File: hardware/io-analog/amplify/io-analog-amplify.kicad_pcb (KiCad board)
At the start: 2 copper layers, 60 x 60 mm, 22 parts, among them J1 IO EXTENSION, J2 DIMMER_B, J5 12V_A, J6 12V_B, U1 LM317T, U2 74LS164, U3 TLC7226A, U4 LM324A

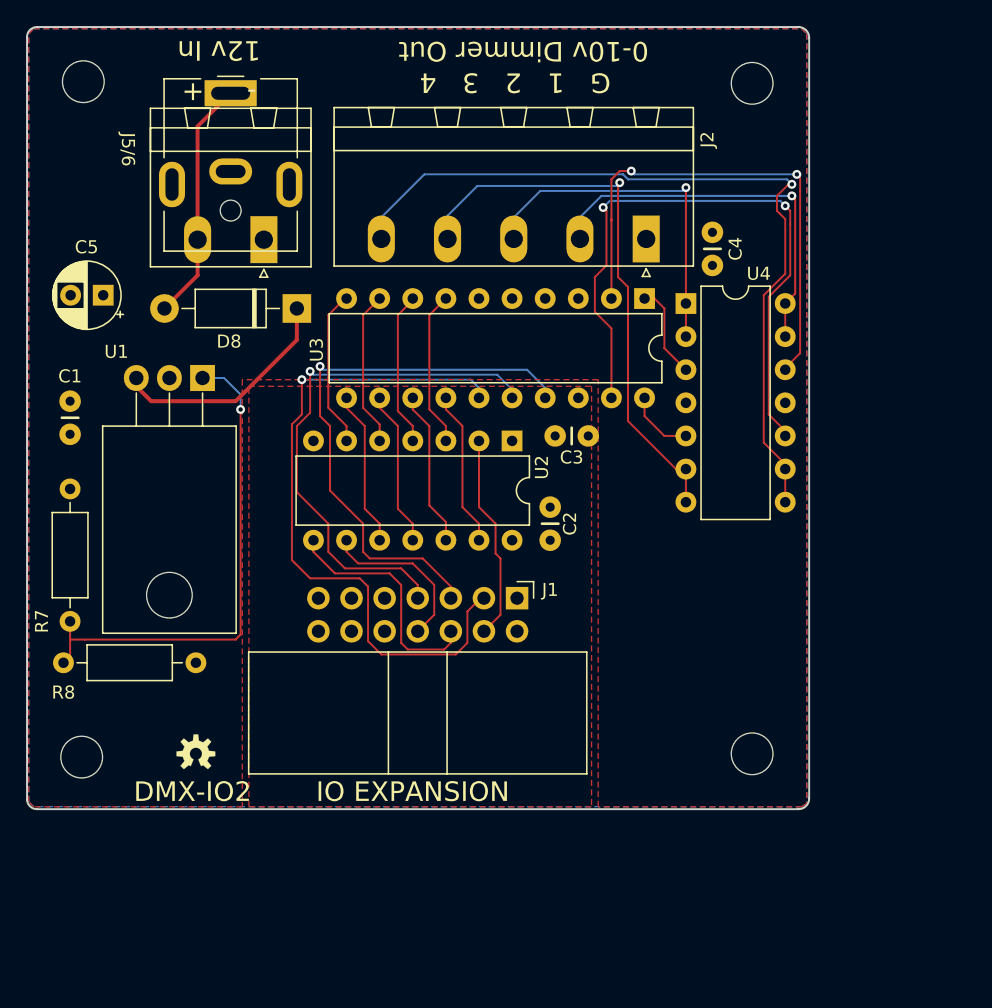
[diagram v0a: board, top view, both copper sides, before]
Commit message: Make io-analog a stackable family io-analog-core handles D to A io-analog-amplify handles voltage output io-analog-pwm handles pwm output for leds, drive display pro io-analog-led handles 5v pwm output for iot, drive display pro
Refactor display-pro to work with io-analog-pwm
Add correct coax power connector
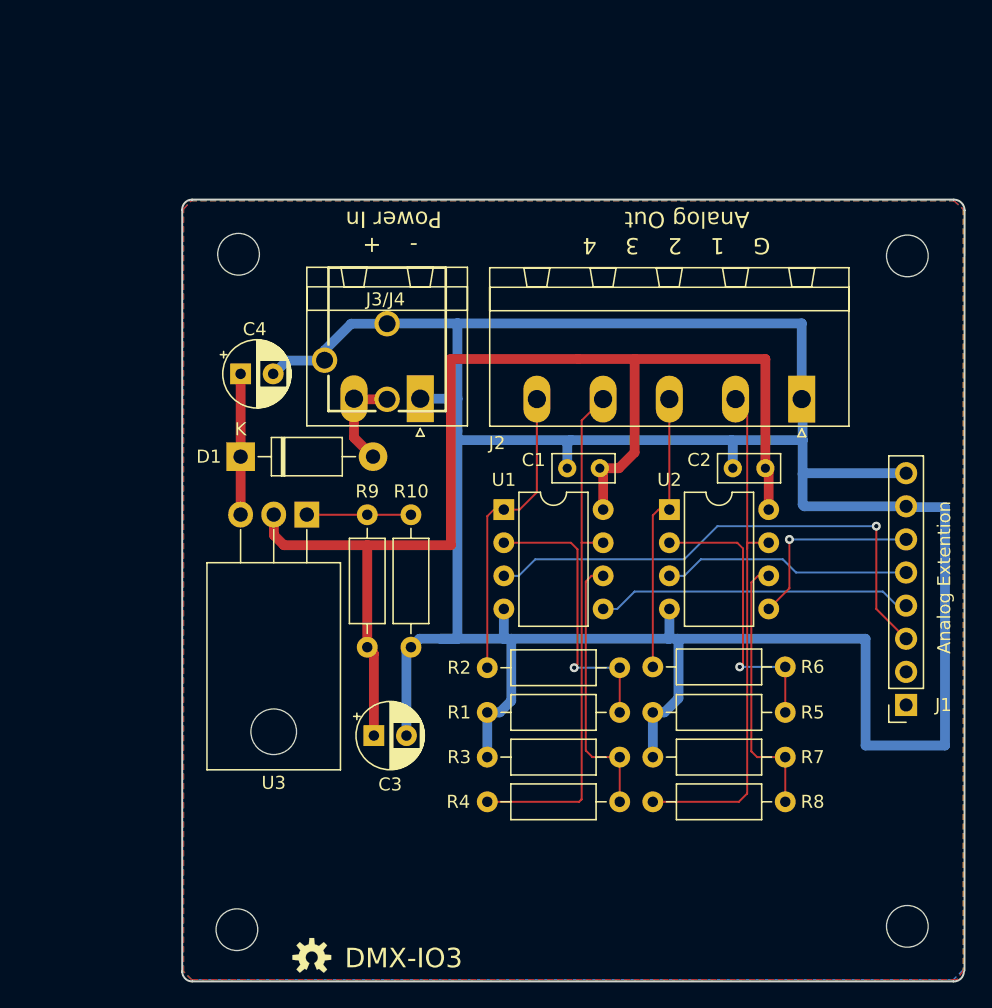
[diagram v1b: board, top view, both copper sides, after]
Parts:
- removed C5: 10uF, Capacitor_THT:CP_Radial_D5.0mm_P2.50mm
- removed D8: 1N5819, Diode_THT:D_DO-41_SOD81_P10.16mm_Horizontal
- removed J5: 12V_A, Connector_BarrelJack:BarrelJack_CUI_PJ-063AH_Horizontal
- removed J6: 12V_B, Connector_Phoenix_MSTB:PhoenixContact_MSTBA_2,5_2-G-5,08_1x02_P5.08mm_Horizontal
- removed U4: LM324A, Package_DIP:DIP-14_W7.62mm
- added D1: 1N5819, Diode_THT:D_DO-41_SOD81_P10.16mm_Horizontal, F.Cu at (130.8, 93.5)
- added J3: Power, Connector_Phoenix_MSTB:PhoenixContact_MSTBA_2,5_2-G-5,08_1x02_P5.08mm_Horizontal, F.Cu at (144.6, 89.1)
- added J4: Power, Connectors:POWER_JACK_PTH_BREAD, F.Cu at (142.0, 75.4)
- added R1: 22.6k 1%, Resistor_THT:R_Axial_DIN0207_L6.3mm_D2.5mm_P10.16mm_Horizontal, F.Cu at (149.7, 113.2)
- added R10: 2.74k 1%, Resistor_THT:R_Axial_DIN0207_L6.3mm_D2.5mm_P10.16mm_Horizontal, F.Cu at (143.9, 108.2)
- added R2: 68.1k 1%, Resistor_THT:R_Axial_DIN0207_L6.3mm_D2.5mm_P10.16mm_Horizontal, F.Cu at (149.7, 109.7)
- added R3: 22.6k 1%, Resistor_THT:R_Axial_DIN0207_L6.3mm_D2.5mm_P10.16mm_Horizontal, F.Cu at (149.7, 116.6)
- added R4: 68.1k 1%, Resistor_THT:R_Axial_DIN0207_L6.3mm_D2.5mm_P10.16mm_Horizontal, F.Cu at (159.9, 120.0)
- added R5: 22.6k 1%, Resistor_THT:R_Axial_DIN0207_L6.3mm_D2.5mm_P10.16mm_Horizontal, F.Cu at (162.4, 113.2)
- added R6: 68.1k 1%, Resistor_THT:R_Axial_DIN0207_L6.3mm_D2.5mm_P10.16mm_Horizontal, F.Cu at (172.6, 109.7)
- added R9: 392 1%, Resistor_THT:R_Axial_DIN0207_L6.3mm_D2.5mm_P10.16mm_Horizontal, F.Cu at (140.5, 98.0)
- C1, C2: value .01uF -> 0.1uF; footprint Capacitors:CAP-PTH-2.54 -> Capacitor_THT:C_Rect_L4.6mm_W2.0mm_P2.50mm_MKS02_FKP02
- C3, C4: value .01uF -> 10uF; footprint Capacitors:CAP-PTH-2.54 -> Capacitor_THT:CP_Radial_D5.0mm_P2.50mm
- J1: value IO EXTENSION -> Analog Extension; footprint Connector_IDC:IDC-Header_2x07_P2.54mm_Horizontal -> Connector_PinSocket_2.54mm:PinSocket_1x08_P2.54mm_Vertical
- J2: value DIMMER_B -> Output
- R7: value 390 -> 22.6k 1%
- R8: value 2.7k -> 68.1k 1%
- U1: value LM317T -> TLV2772; footprint Package_TO_SOT_THT:TO-220-3_Horizontal_TabDown -> Package_DIP:DIP-8_W7.62mm
- U2: value 74LS164 -> TLV2772; footprint Package_DIP:DIP-14_W7.62mm -> Package_DIP:DIP-8_W7.62mm
- U3: value TLC7226A -> LM317T; footprint Package_DIP:DIP-20_W7.62mm -> Package_TO_SOT_THT:TO-220-3_Horizontal_TabDown
- moved R8 46.5 mm to (172.6, 120.0)
- moved R7 45.9 mm to (162.4, 116.6), turned to 0 degrees
- moved C1 40.8 mm to (158.4, 94.4), turned to 180 degrees
- moved C4 37.4 mm to (130.8, 87.2), turned to 0 degrees
- moved J1 30.9 mm to (181.9, 112.6), turned to 180 degrees
- moved U3 30.8 mm to (135.9, 98.0), turned to 180 degrees
- moved C3 27.5 mm to (141.0, 114.9)
- moved U1 25.2 mm to (151.0, 97.6), turned to 0 degrees
- moved ? 18.0 mm to (136.3, 132.0)
- moved MH4 17.8 mm to (182.0, 129.6)
- moved MH1 17.8 mm to (130.7, 78.0)
- moved MH3 17.8 mm to (130.5, 129.8)
- moved MH2 17.8 mm to (182.0, 78.1)
- moved J2 17.1 mm to (173.9, 89.1)
- moved C2 17.0 mm to (171.1, 94.4), turned to 180 degrees
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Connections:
- C1 pad 1: +10V -> Net-(C1-Pad1)
- C2 pad 1: +5V -> Net-(C1-Pad1)
- C3 pad 1: +5V -> Net-(C1-Pad1)
- C4 pad 1: +10V -> Net-(C4-Pad1)
- J1 pad 1: +5V -> Net-(J1-Pad1)
- J1 pad 2: +5V -> Net-(J1-Pad2)
- J1 pad 3: /~WR -> /AO3
- J1 pad 4: /SR-OUT -> /AO2
- J1 pad 5: /A0 -> /AO1
- J1 pad 6: /SR-CLK -> /AO0
- J1 pad 7: /A1 -> GND
- J1 pad 8: /~SR_CLR -> GND
- R7 pad 1: Net-(R7-Pad1) -> GND
- R7 pad 2: +10V -> Net-(R7-Pad2)
- R8 pad 1: GND -> Net-(R7-Pad2)
- R8 pad 2: Net-(R7-Pad1) -> Net-(J2-Pad2)
- U1 pad 1: Net-(R7-Pad1) -> Net-(J2-Pad5)
- U1 pad 2: +10V -> Net-(R1-Pad2)
- U1 pad 3: Net-(D8-Pad1) -> /AO3
- U2 pad 1: +5V -> Net-(J2-Pad3)
- U2 pad 2: /SR-OUT -> Net-(R5-Pad2)
- U2 pad 3: /D7 -> /AO1
- U2 pad 4: /D6 -> GND
- U2 pad 5: /D5 -> /AO0
- U2 pad 6: /D4 -> Net-(R7-Pad2)
- U2 pad 7: GND -> Net-(J2-Pad2)
- U2 pad 8: /SR-CLK -> Net-(C1-Pad1)
- U3 pad 1: /AO1 -> Net-(R10-Pad2)
- U3 pad 2: /AO0 -> Net-(C1-Pad1)
- U3 pad 3: GND -> Net-(C4-Pad1)
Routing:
- net GND: track 0.00 -> 235.2 mm
- net Net-(C1-Pad1): track 0.00 -> 94.3 mm
- net /~WR: track 52.4 -> 0.00 mm, vias 1 -> 0
- net /A0: track 43.0 -> 0.00 mm, vias 1 -> 0
- net /A1: track 40.9 -> 0.00 mm, vias 1 -> 0
- net Net-(R7-Pad1): track 38.5 -> 0.00 mm, vias 1 -> 0
- net Net-(J2-Pad5): track 61.5 -> 23.5 mm, vias 1 -> 0
- net /AO0: track 39.4 -> 14.9 mm, vias 2 -> 1
- net Net-(R5-Pad2): track 0.00 -> 22.0 mm, vias 0 -> 1
- net Net-(R1-Pad2): track 0.00 -> 22.0 mm, vias 0 -> 1
- net Net-(R7-Pad2): track 0.00 -> 20.7 mm
- net Net-(R3-Pad2): track 0.00 -> 20.7 mm
- net /AO2: track 5.20 -> 24.2 mm
- net Net-(D8-Pad2): track 18.6 -> 0.00 mm
- net /SR-CLK: track 18.2 -> 0.00 mm
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- added copper zone on F.Cu, net Net-(C1-Pad1)
- removed copper zone on F.Cu, net +10V
- removed copper zone on F.Cu, net +5V
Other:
- outline, holes or cut-outs redrawn
- net class Power: clearance 0.1524 -> 0.25; trace_width 0.3048 -> 0.75
- board text added: "- + Power In"
- board text added: "Analog Extention"
- board text added: "DMX-IO3"
- board text added: "DMX-IO3, Rev 1.2 Crazy Giraffe Software"
- board text added: "G 1 2 3 4 Analog Out"
- board text added: "J3/J4"
- board text removed: "- +"
- board text removed: "12v In"
- board text removed: "DMX-IO2"
- board text removed: "DMX-IO2, Rev 1.1 Crazy Giraffe Software"
- board text removed: "G 1 2 3 4 0-10v Dimmer Out"
- board text removed: "IO EXPANSION"
- board text removed: "J5/6"
